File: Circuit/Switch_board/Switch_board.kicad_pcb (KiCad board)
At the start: 2 copper layers, 17 parts, among them J1 switch_mode, J2 switch, P1 XT30, Q1 BSS138, Q2 BSS138, U1 DRV5023

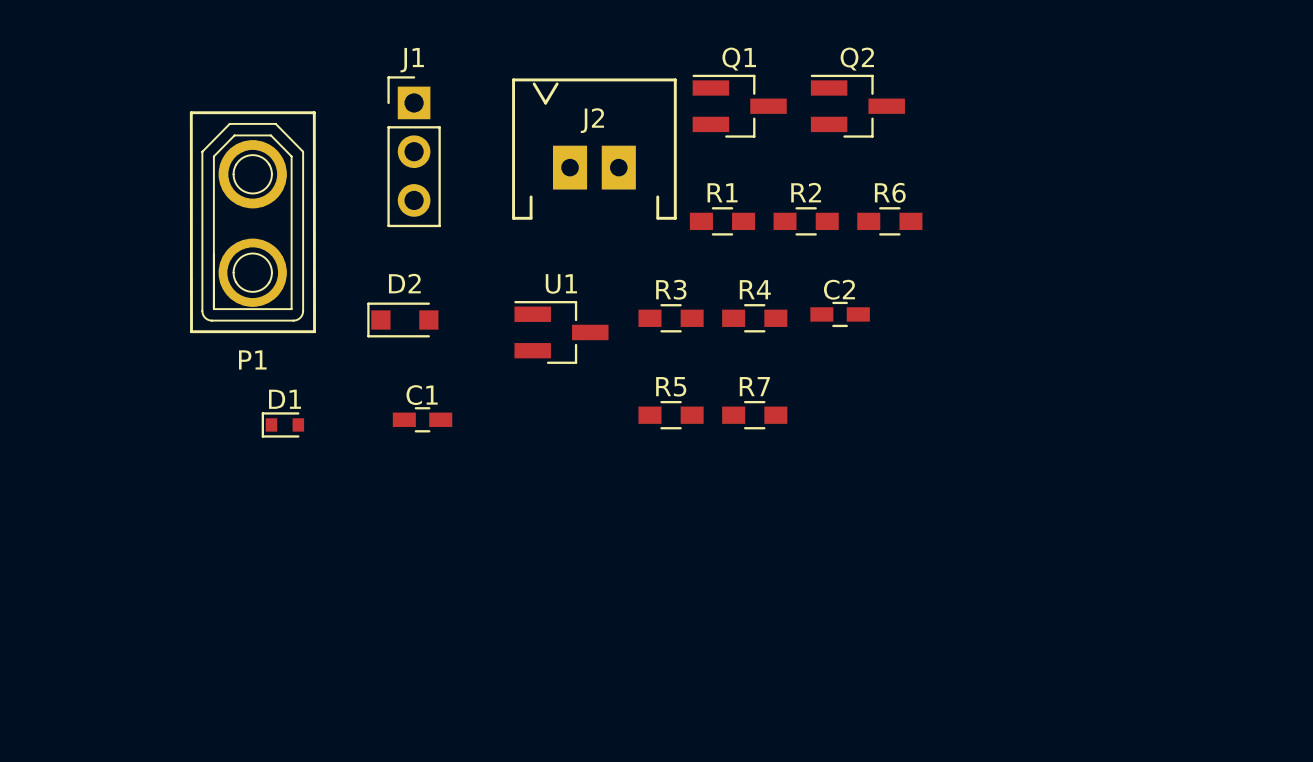
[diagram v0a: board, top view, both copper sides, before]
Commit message: imported footprints of components of Switch_board into pcb and set design rules
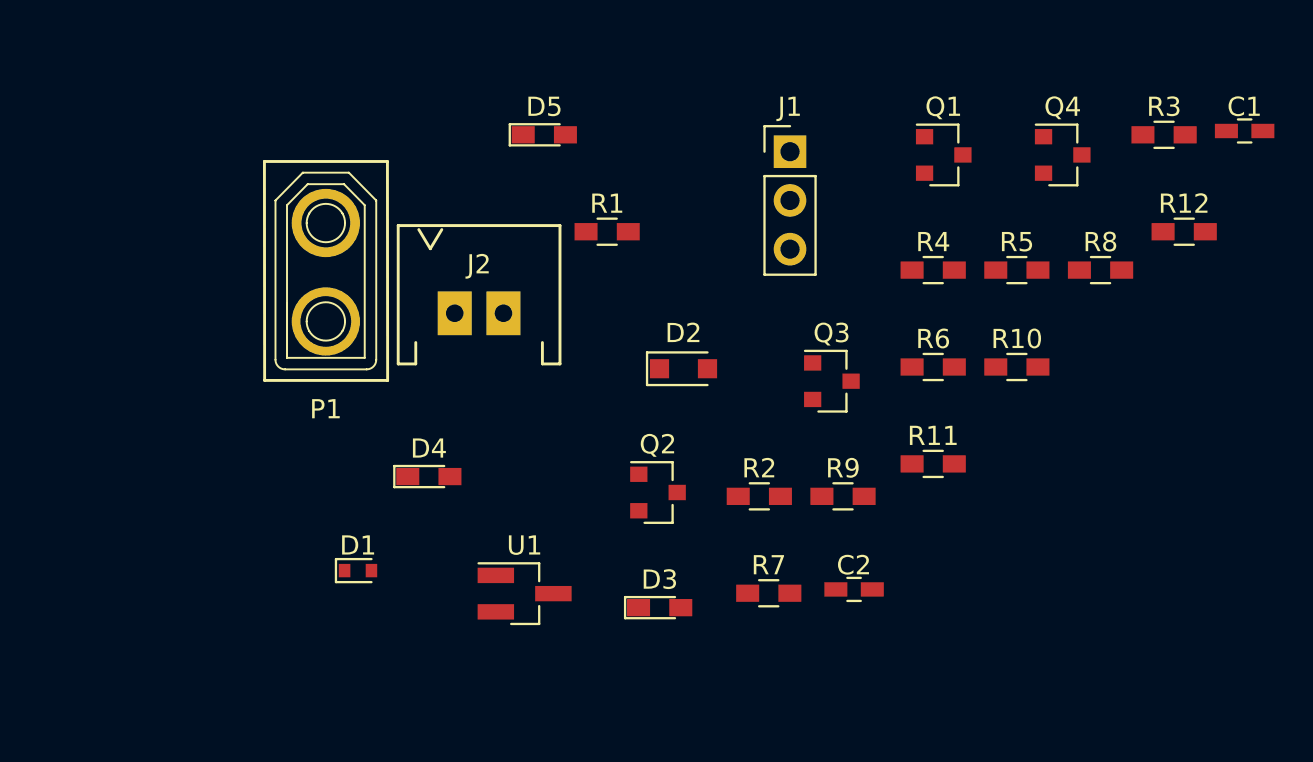
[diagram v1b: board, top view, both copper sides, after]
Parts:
- added D3: LED_PWR, LEDs:LED_0603_HandSoldering, F.Cu at (172.0, 133.7)
- added D4: LED_HALL_SENSOR_OUT, LEDs:LED_0603_HandSoldering, F.Cu at (160.0, 126.9)
- added D5: LED_IS_SWITCH_HIGH, LEDs:LED_0603_HandSoldering, F.Cu at (166.0, 109.1)
- added Q3: 2N7002, TO_SOT_Packages_SMD:SOT-23, F.Cu at (181.0, 121.9)
- added Q4: 2N7002, TO_SOT_Packages_SMD:SOT-23, F.Cu at (193.0, 110.2)
- added R10: 1k, Resistors_SMD:R_0603_HandSoldering, F.Cu at (190.6, 121.2)
- added R11: 4.7k, Resistors_SMD:R_0603_HandSoldering, F.Cu at (186.3, 126.3)
- added R12: 1k, Resistors_SMD:R_0603_HandSoldering, F.Cu at (199.3, 114.2)
- added R8: 4.7k, Resistors_SMD:R_0603_HandSoldering, F.Cu at (195.0, 116.2)
- added R9: 4.7k, Resistors_SMD:R_0603_HandSoldering, F.Cu at (181.6, 127.9)
- Q1, Q2: value BSS138 -> 2N7002; footprint TO_SOT_Packages_SMD:SOT-23_Handsoldering -> TO_SOT_Packages_SMD:SOT-23
- R2, R5: value 10k -> 1M
- R7: value 4.7k -> 2.2k
- moved C1 45.4 mm to (202.5, 108.9)
- moved R3 27.4 mm to (198.3, 109.1)
- moved Q2 22.7 mm to (171.9, 127.7)
- moved J1 19.8 mm to (178.8, 110.0)
- moved R5 19.5 mm to (190.6, 116.2)
- moved D2 14.7 mm to (173.2, 121.3)
- moved R2 14.5 mm to (177.2, 127.9)
- moved C2 14.3 mm to (182.1, 132.8)
- moved U1 13.7 mm to (165.0, 133.0)
- moved Q1 10.9 mm to (186.8, 110.2)
- moved J2 9.68 mm to (162.6, 118.4)
- moved R4 9.63 mm to (186.3, 116.2)
- moved R7 9.31 mm to (177.7, 133.0)
- moved D1 8.49 mm to (156.3, 131.8)
- moved R6 7.92 mm to (186.3, 121.2)
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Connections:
- net Net-(C2-Pad1) renamed hall_sensor_out
- D2 pad 1: Net-(D2-Pad1) -> +switch
- J2 pad 1: Net-(D2-Pad1) -> +switch
- Q1 pad 3: Net-(J1-Pad3) -> Net-(D4-Pad1)
- Q2 pad 3: Net-(D2-Pad1) -> Net-(D5-Pad1)
- R3 pad 2: Net-(Q1-Pad1) -> Net-(Q3-Pad1)
- R6 pad 2: Net-(Q2-Pad1) -> Net-(Q4-Pad1)
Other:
- net class Default: clearance 0.2 -> 0.254; trace_width 0.25 -> 0.254; via_dia 0.6 -> 1.1176; via_drill 0.4 -> 0.6096
- rule trace_clearance: 0.2 -> 0.254
- rule trace_min: 0.2 -> 0.254
- rule via_min_drill: 0.3 -> 0.6096
- rule via_min_size: 0.4 -> 1.1176

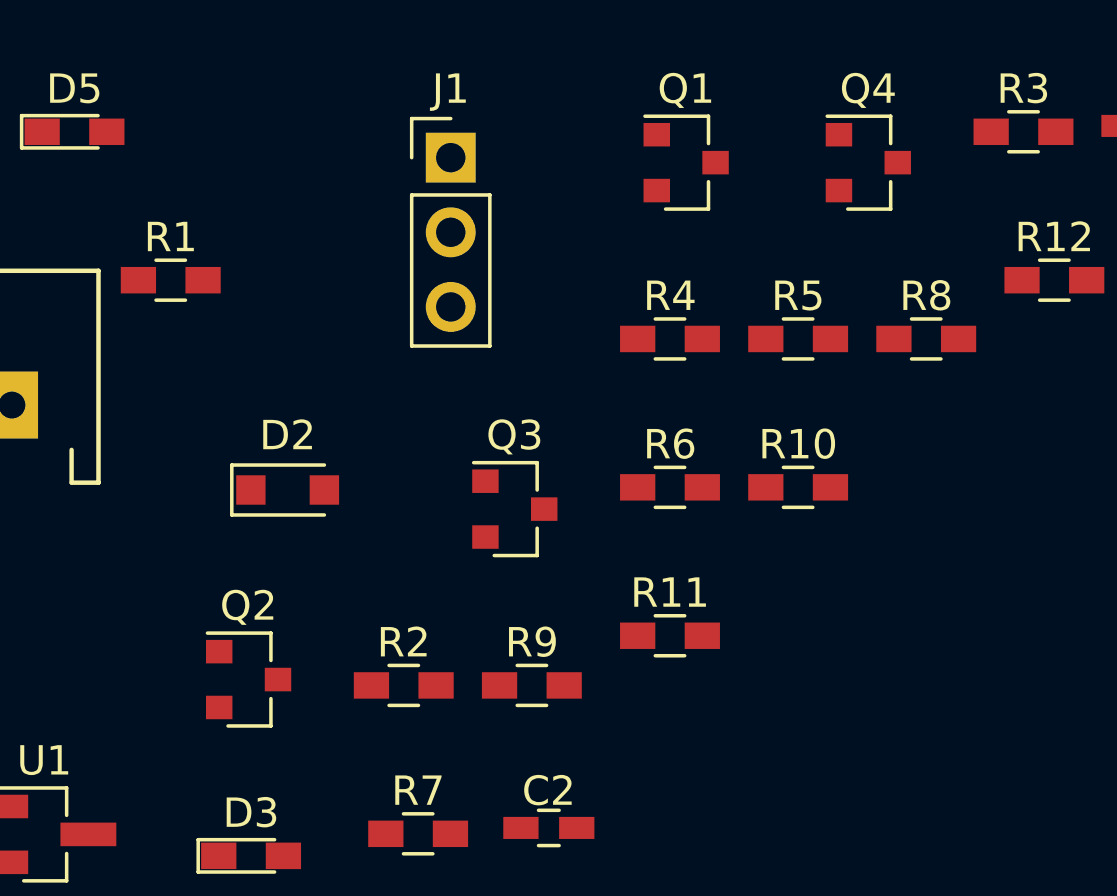
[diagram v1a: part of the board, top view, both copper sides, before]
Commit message: changed SOT-23 footprints on Switch_board to SOT-23_handsoldering footprints
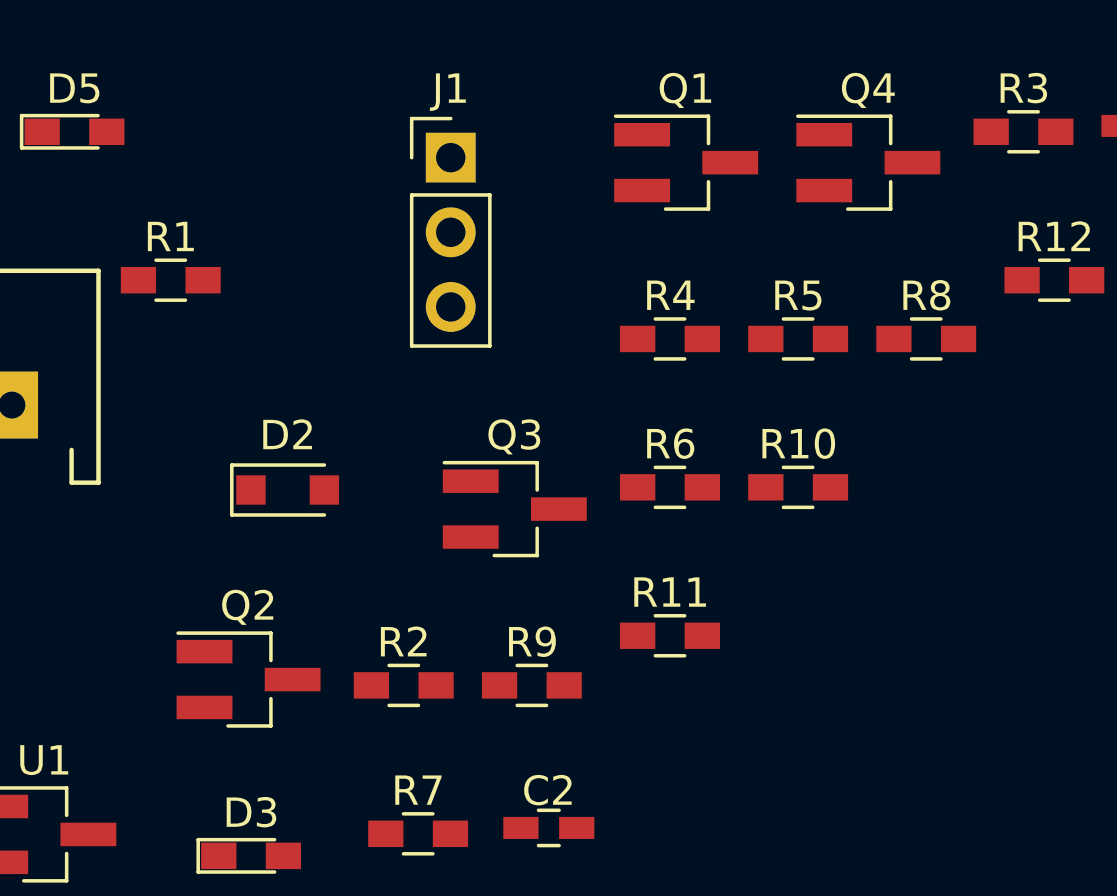
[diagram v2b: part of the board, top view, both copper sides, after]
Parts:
- Q1, Q2, Q3, Q4: footprint TO_SOT_Packages_SMD:SOT-23 -> TO_SOT_Packages_SMD:SOT-23_Handsoldering

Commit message: pcb layout of Switch_board was drafted
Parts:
- added REF**: MountingHole_3mm, Mounting_Holes:MountingHole_3mm, F.Cu at (143.5, 135.9)
- added REF**: MountingHole_3mm, Mounting_Holes:MountingHole_3mm, F.Cu at (143.5, 111.8)
- added REF**: MountingHole_3mm, Mounting_Holes:MountingHole_3mm, F.Cu at (186.7, 111.8)
- added REF**: MountingHole_3mm, Mounting_Holes:MountingHole_3mm, F.Cu at (186.7, 135.9)
- C1, C2, R1, U1: moved to B.Cu
- moved R3 46.2 mm to (157.5, 130.8), turned to 90 degrees
- moved C1 43.7 mm to (161.3, 123.5), turned to 270 degrees
- moved R8 43.3 mm to (151.8, 119.2), turned to 270 degrees
- moved Q1 40.3 mm to (152.1, 130.6), turned to 90 degrees
- moved R10 33.3 mm to (157.5, 124.6), turned to 90 degrees
- moved D3 29.3 mm to (151.8, 112.6), turned to 270 degrees
- moved R11 27.8 mm to (159.4, 119.2), turned to 270 degrees
- moved R9 27.4 mm to (155.6, 119.2), turned to 270 degrees
- moved R4 26.6 mm to (162.6, 128.3)
- moved J1 26.0 mm to (176.5, 135.9), turned to 270 degrees
- moved R5 25.4 mm to (170.3, 131.4), turned to 180 degrees
- moved R2 23.1 mm to (155.7, 136.5), turned to 180 degrees
- moved J2 22.2 mm to (184.2, 123.8), turned to 270 degrees
- moved Q4 21.9 mm to (175.9, 123.8), turned to 90 degrees
- moved Q3 20.8 mm to (163.4, 133.0)
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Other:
- board outline added: 50.8 x 31.7 mm
